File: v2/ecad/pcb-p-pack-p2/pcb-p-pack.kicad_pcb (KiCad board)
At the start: 2 copper layers, 70 x 44 mm, 60 parts, among them Q1 CSD17570Q5B 30 V N-FET, charg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, Q2 CSD17570Q5B 30 V N-FET, disch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, U1 BQ4050RSMR: SMBus 1.1 gas gau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

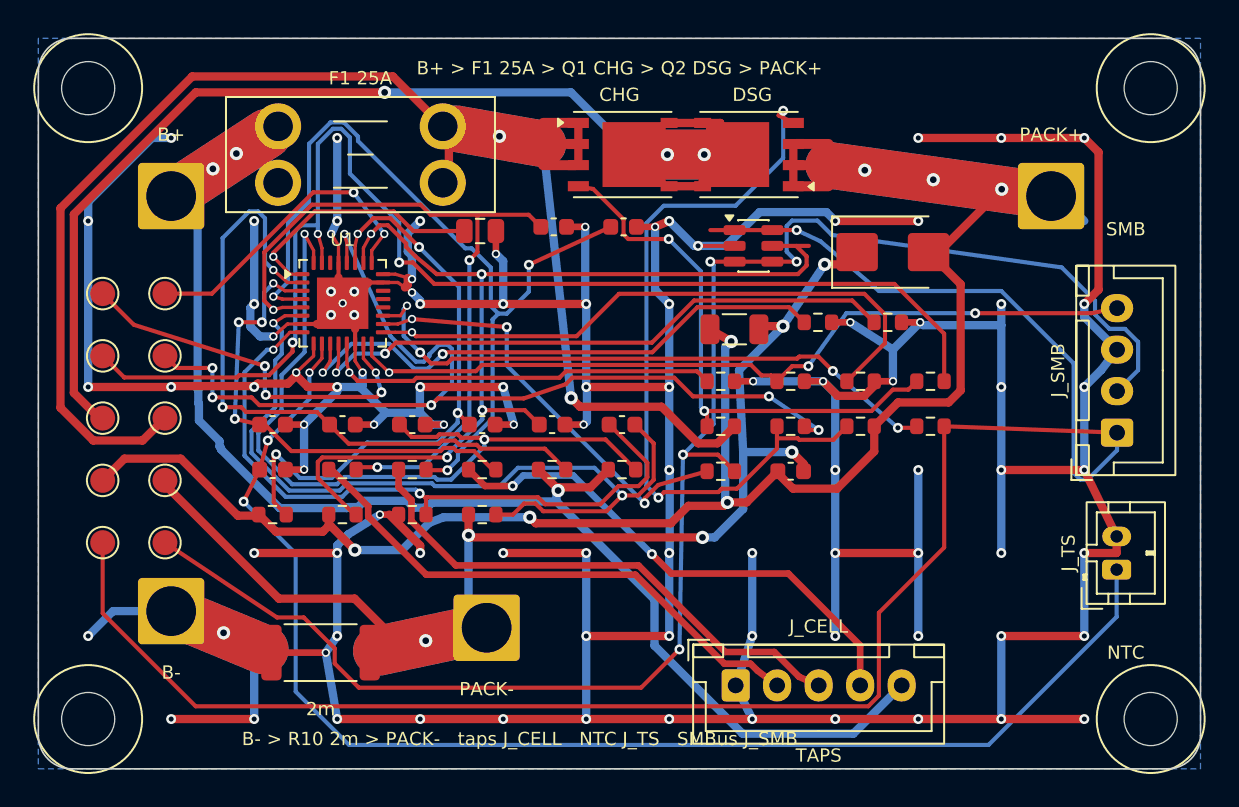
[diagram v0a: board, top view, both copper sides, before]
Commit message: feat(pcb-p): P3 is re-cut, and every part on it is orderable [MESHSAT-862]
routeflow ended CLEAN: hard 0, unrouted 0, 55 vias, board sha256 5ae0ce7e matching the deliverable's own
record.

It took four attempts and each one was refused for a different reason, every one of them real:

  1  a blank BOM code, because the thermistor row's comment reword stopped matching an lcsc-allow line
     that should never have covered a socket in the first place
  2  a locked GND via dead at its B.Cu end, and the tool written for exactly that refused to touch it
     because two tracks landed on it, both on F.Cu
  3  the same defect at a different via, because the exposed pad of the BQ4050 had one thermal via
     instead of four and the fill had retreated from it
  4  the pruner declared at the top level of boards/p.json, where finish.sh cannot see it

jlc_certify on P: 19 components, 19 CERTIFIED, nothing hand-fit, nothing bench-fitted, nothing open.
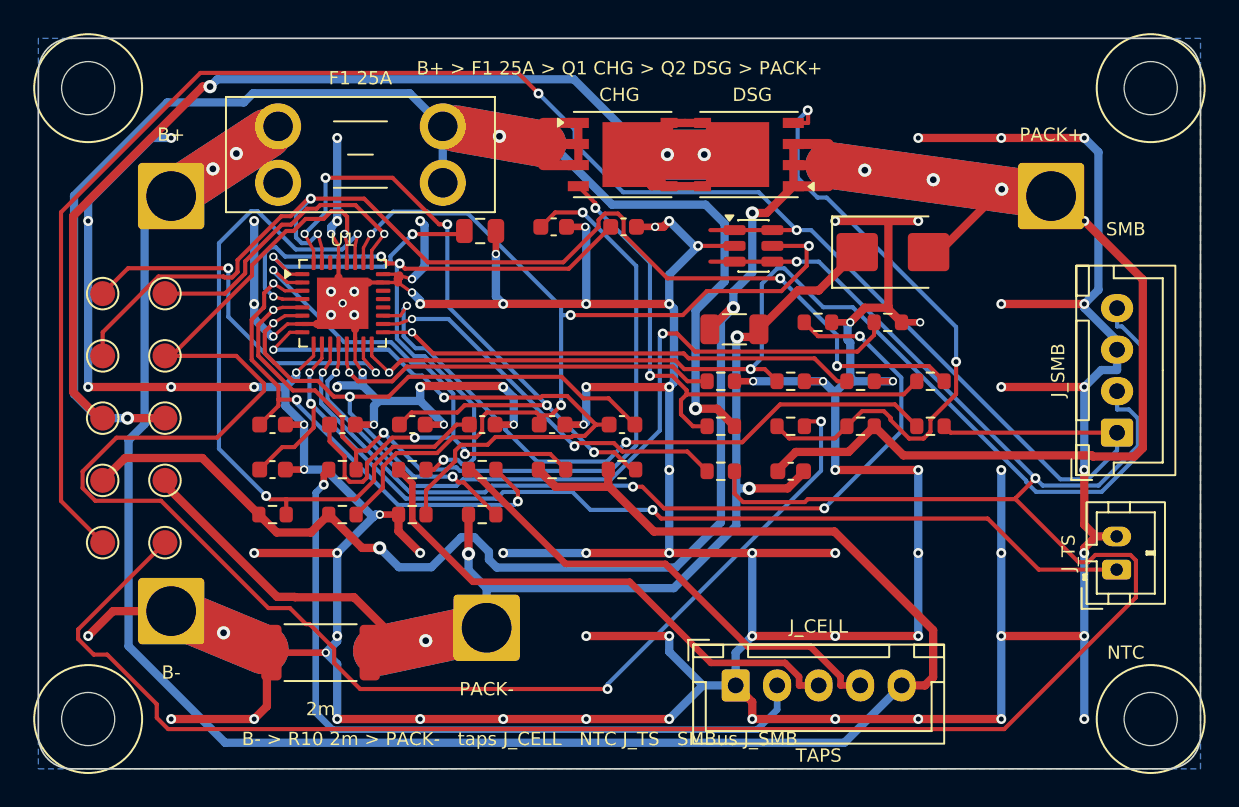
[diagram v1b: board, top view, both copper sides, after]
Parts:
- J_TS: value cell thermistor (JST-PH 1x2): the 103AT in the block -> JST-PH 1x2 socket for the cell thermistor lead (the 10k NTC, a 103AT, sits in the cell block)
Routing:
- net /SMBD: track 98.5 -> 145.9 mm, vias 4 -> 2
- net /CELL4: track 91.4 -> 130.2 mm, vias 3 -> 2
- net /DSG_R: track 61.5 -> 98.6 mm, vias 6 -> 3
- net /PACK_P: track 126.2 -> 152.2 mm
- net /PRES: track 48.7 -> 71.3 mm, vias 3 -> 2
- net /TS2: track 34.1 -> 54.1 mm, vias 2 -> 4
- net /TS1: track 80.7 -> 62.7 mm
- net /CELL1: track 32.7 -> 45.1 mm, vias 0 -> 1
- net /TS3: track 36.5 -> 47.4 mm
- net /SRN_F: track 49.9 -> 41.3 mm, vias 2 -> 3
- net /PACK_F: track 36.1 -> 44.3 mm, vias 4 -> 2
- net /DSG_G: track 45.2 -> 37.3 mm
- net /VC1_F: track 44.5 -> 52.2 mm
- net /DISP: track 36.9 -> 29.2 mm
- net /VC2_F: track 51.5 -> 44.6 mm, vias 3 -> 4
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
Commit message: feat(pcb-p): P4 is cut, 0 hard, 0 unrouted, 3 of 3 rails MET [MESHSAT-862]
The first deliverable of the density pass. verify_deliverable ALL PASS on 36 of 36 properties, seventeen
items, the board sha256 d79865e7 matching three ways: the box, this project copy and the folder's own record.

What changed from P3, all of it because the corrected density measure asked for it: the pack current enters
its bands through three 1.2 mm source runs instead of 0.6 mm, each FET's three source tracks carry two
0.9/0.5 vias at the one place the current must change layer, and the bands' stitch is three across at 1.0 mm
instead of three along at 1.6. PACK_P's worst conductor was 4.16 A against IPC's 2.73 and is now 1.43 against
2.39; FUSED's 193.2 A/mm2 of owner ruling 7 was an artefact of the broken measure and is gone with it.

check_contracts is 42 of 42 across the set.
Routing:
- net /SRN_F: track 41.3 -> 68.0 mm, vias 3 -> 4
- net /CELL4: track 130.2 -> 104.7 mm, vias 2 -> 9
- net /DSG_R: track 98.6 -> 74.2 mm, vias 3 -> 4
- net /SMBD: track 145.9 -> 121.8 mm, vias 2 -> 5
- net /TS2: track 54.1 -> 77.6 mm, vias 4 -> 2
- net /PRES: track 71.3 -> 48.9 mm
- net /TS1: track 62.7 -> 79.7 mm
- net /VC1_F: track 52.2 -> 37.0 mm, vias 3 -> 4
- net /FUSED: track 95.0 -> 105.1 mm, vias 3 -> 6
- net /CHG_R: track 71.0 -> 81.1 mm
- net /PACK_F: track 44.3 -> 34.5 mm, vias 2 -> 3
- net /DSG_G: track 37.3 -> 27.7 mm
- net /BAT_F: track 44.0 -> 35.7 mm, vias 5 -> 3
- net /SMBC_I: track 39.8 -> 47.8 mm, vias 2 -> 4
- net GND: track 441.6 -> 448.7 mm, vias 95 -> 97
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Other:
- board text added: "PCB-P PACK BMS REV A (P4)"
- board text removed: "PCB-P PACK BMS REV A (P3)"
